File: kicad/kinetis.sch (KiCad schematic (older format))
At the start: 25 parts, among them J1 USB_Micro_B, J2 FTDI_Connector, U1 MKL16Z64VLH4, U2 LM1117-ADJ

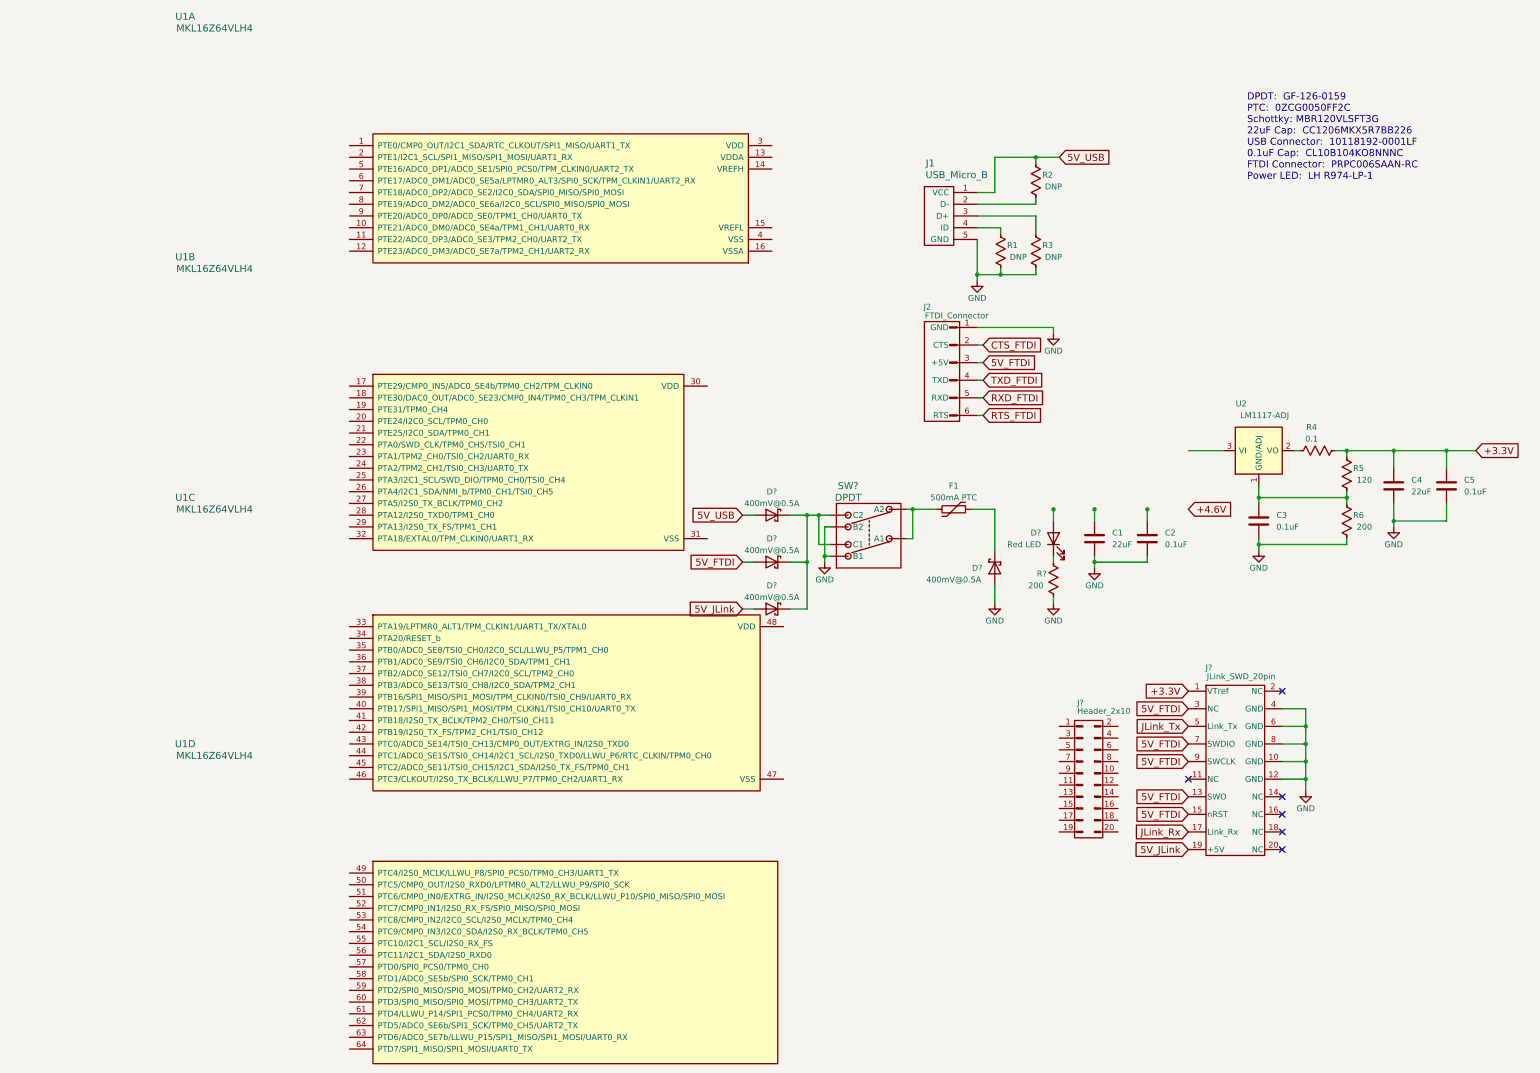
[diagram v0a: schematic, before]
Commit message: Updated schematic. Reworked Kinetis symbol. Connected LEDs.
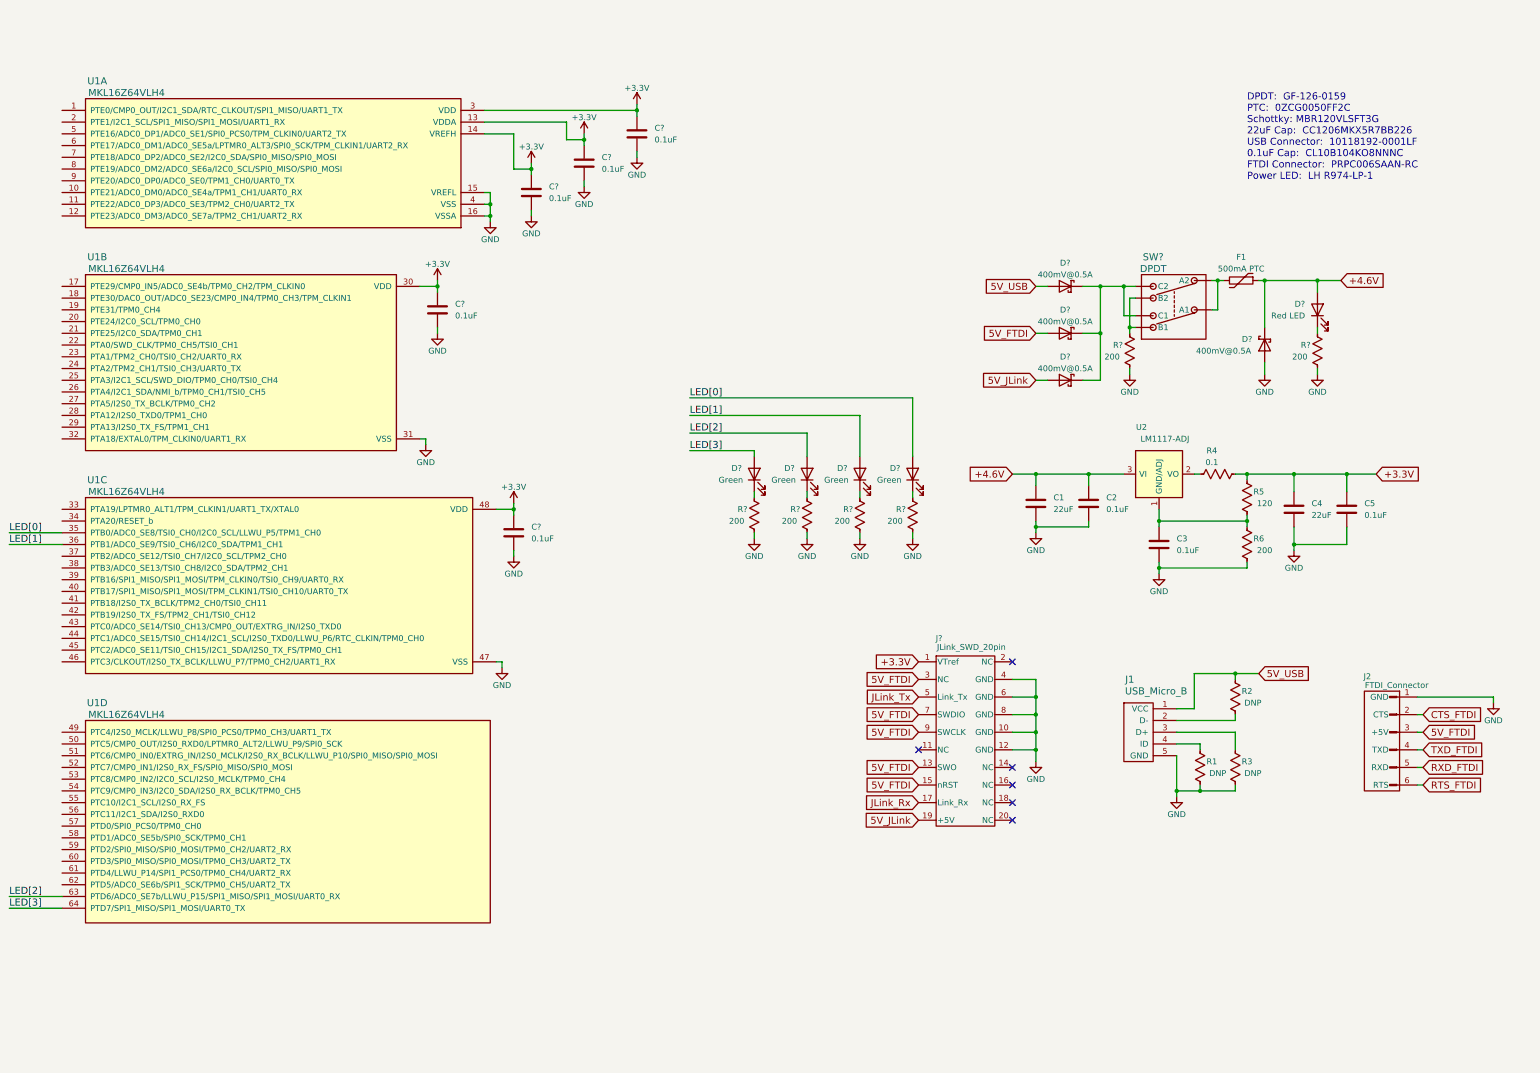
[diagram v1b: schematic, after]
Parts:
- removed J?: Header_2x10, symbol Header_2x10
- added C? (x5): 0.1uF, symbol C
- added D? (x4): Green, symbol LED_AK
- added R? (x5): 200, symbol R_US
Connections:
- net +4.6V: now also C1.1, C2.1, D?.A, D?.K, F1.1, U2.3 (VI)
- net GND: now also U1.15 (VREFL), U1.16 (VSSA), U1.31 (VSS), U1.4 (VSS), U1.47 (VSS), C?.2, C?.2, C?.2, C?.2, C?.2, R?.1, R?.1, R?.1, R?.1, R?.1; no longer SW?.~ (C2)
- net +3V3: now reaches U1.13 (VDDA)
- net +3V3: now also U1.14 (VREFH), U1.3 (VDD), U1.30 (VDD), U1.48 (VDD), C?.1, C?.1, C?.1, C?.1, C?.1
- net LED[0]: now reaches U1.35 (PTB0/ADC0_SE8/TSI0_CH0/I2C0_SCL/LLWU_P5/TPM1_CH0)
- net LED[0]: now also D?.A
- net LED[1]: now reaches U1.36 (PTB1/ADC0_SE9/TSI0_CH6/I2C0_SDA/TPM1_CH1)
- net LED[1]: now also D?.A
- net LED[2]: now reaches U1.63 (PTD6/ADC0_SE7b/LLWU_P15/SPI1_MISO/SPI1_MOSI/UART0_RX)
- net LED[2]: now also D?.A
- net LED[3]: now reaches U1.64 (PTD7/SPI1_MISO/SPI1_MOSI/UART0_TX)
- net LED[3]: now also D?.A
- new net: R?.2, SW?.~ (C2)
- new net: D?.K, R?.2 (x4)
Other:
- moved on the sheet: C1, C2, C3, C4, C5, D?, F1, J1, J2, J?, R1, R2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

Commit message: Lots of changes.
Added clock crystal and load capacitors. Added 16-pin headers to
each side of the microcontroller. Added user pushbuttons and also
a reset pushbutton.
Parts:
- added C6, C7: 27pF, symbol C
- added J1, J2, J3, J4: CONN_01X16, symbol CONN_01X16
- added R1, R10, R11, R12, R13, R14, R2, R3, R4, R5, R6, R7, R8, R9: 0.0, symbol R_US
- added R15, R25, R26, R31, R32: 10k, symbol R_US
- added R16: 120, symbol R_US
- added SW1, SW3, SW4, SW5, SW6: SPST, symbol SPST
- added Y1: 12 MHz, symbol Crystal
- gave numbers to parts that had none: 22
- renumbered C3 to C10, C4 to C11, C5 to C12, C1 to C8, C2 to C9, J1 to J6, J2 to J7, R1 to R21, R2 to R23, R3 to R24, R4 to R27, R5 to R28, R6 to R29
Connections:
- net +3.3V: now also J1.13 (P13), J1.14 (P14), J1.3 (P3), J2.14 (P14), J3.16 (P16)
- net +3V3: now also R15.1, SW3.3, SW3.4, SW4.3, SW4.4, SW5.3, SW5.4, SW6.3, SW6.4
- net 5V_FTDI: no longer J5.13 (SWO), J5.15 (nRST), J5.3 (NC), J5.7 (SWDIO), J5.9 (SWCLK)
- net CTS_FTDI: now also R3.2
- net GND: now also C6.2, C7.2, J1.15 (P15), J1.16 (P16), J1.4 (P4), J2.15 (P15), J3.15 (P15), R25.2, R26.2, R31.2, R32.2, SW1.1, SW1.2
- net JLink_Rx: now also R12.2
- net JLink_Tx: now also R11.2
- net LED[0]: now also R5.2; no longer U1.35 (PTB0/ADC0_SE8/TSI0_CH0/I2C0_SCL/LLWU_P5/TPM1_CH0)
- net LED[1]: now also R6.2; no longer U1.36 (PTB1/ADC0_SE9/TSI0_CH6/I2C0_SDA/TPM1_CH1)
- net LED[2]: now also R13.2; no longer U1.63 (PTD6/ADC0_SE7b/LLWU_P15/SPI1_MISO/SPI1_MOSI/UART0_RX)
- net LED[3]: now also R14.2; no longer U1.64 (PTD7/SPI1_MISO/SPI1_MOSI/UART0_TX)
- net RTS_FTDI: now also R4.2
- net RXD_FTDI: now also R1.2
- net TXD_FTDI: now also R2.2
- net HEADER_A[1]: now reaches U1.1 (PTE0/CMP0_OUT/I2C1_SDA/RTC_CLKOUT/SPI1_MISO/UART1_TX)
- net HEADER_A[1]: now also J1.1 (P1)
- net HEADER_A[10]: now reaches U1.10 (PTE21/ADC0_DM0/ADC0_SE4a/TPM1_CH1/UART0_RX)
- net HEADER_A[10]: now also J1.10 (P10), R2.1
- net HEADER_A[11]: now reaches U1.11 (PTE22/ADC0_DP3/ADC0_SE3/TPM2_CH0/UART2_TX)
- net HEADER_A[11]: now also J1.11 (P11)
- net HEADER_A[12]: now reaches U1.12 (PTE23/ADC0_DM3/ADC0_SE7a/TPM2_CH1/UART2_RX)
- net HEADER_A[12]: now also J1.12 (P12)
- net HEADER_A[2]: now reaches U1.2 (PTE1/I2C1_SCL/SPI1_MISO/SPI1_MOSI/UART1_RX)
- net HEADER_A[2]: now also J1.2 (P2)
- net HEADER_A[5]: now reaches U1.5 (PTE16/ADC0_DP1/ADC0_SE1/SPI0_PCS0/TPM_CLKIN0/UART2_TX)
- net HEADER_A[5]: now also J1.5 (P5)
- net HEADER_A[6]: now reaches U1.6 (PTE17/ADC0_DM1/ADC0_SE5a/LPTMR0_ALT3/SPI0_SCK/TPM_CLKIN1/UART2_RX)
- net HEADER_A[6]: now also J1.6 (P6)
- net HEADER_A[7]: now reaches U1.7 (PTE18/ADC0_DP2/ADC0_SE2/I2C0_SDA/SPI0_MISO/SPI0_MOSI)
- net HEADER_A[7]: now also J1.7 (P7)
- net HEADER_A[8]: now reaches U1.8 (PTE19/ADC0_DM2/ADC0_SE6a/I2C0_SCL/SPI0_MISO/SPI0_MOSI)
- net HEADER_A[8]: now also J1.8 (P8)
- net HEADER_A[9]: now reaches U1.9 (PTE20/ADC0_DP0/ADC0_SE0/TPM1_CH0/UART0_TX)
- net HEADER_A[9]: now also J1.9 (P9), R1.1
- net HEADER_B[1]: now reaches U1.17 (PTE29/CMP0_IN5/ADC0_SE4b/TPM0_CH2/TPM_CLKIN0)
- net HEADER_B[1]: now also J2.1 (P1)
- net HEADER_B[2]: now reaches U1.18 (PTE30/DAC0_OUT/ADC0_SE23/CMP0_IN4/TPM0_CH3/TPM_CLKIN1)
- net HEADER_B[2]: now also J2.2 (P2)
- net HEADER_B[3]: now reaches U1.19 (PTE31/TPM0_CH4)
- net HEADER_B[3]: now also J2.3 (P3)
- net HEADER_B[4]: now reaches U1.20 (PTE24/I2C0_SCL/TPM0_CH0)
- net HEADER_B[4]: now also J2.4 (P4)
- net HEADER_B[5]: now reaches U1.21 (PTE25/I2C0_SDA/TPM0_CH1)
- net HEADER_B[5]: now also J2.5 (P5)
- net JLink_SWCLK: now reaches U1.22 (PTA0/SWD_CLK/TPM0_CH5/TSI0_CH1)
- net JLink_SWCLK: now also J5.9 (SWCLK)
- net HEADER_B[7]: now reaches U1.23 (PTA1/TPM2_CH0/TSI0_CH2/UART0_RX)
- net HEADER_B[7]: now also J2.7 (P7)
- net HEADER_B[8]: now reaches U1.24 (PTA2/TPM2_CH1/TSI0_CH3/UART0_TX)
- net HEADER_B[8]: now also J2.8 (P8)
- net JLink_SWDIO: now reaches U1.25 (PTA3/I2C1_SCL/SWD_DIO/TPM0_CH0/TSI0_CH4)
- net JLink_SWDIO: now also J5.7 (SWDIO)
- net HEADER_B[10]: now reaches U1.26 (PTA4/I2C1_SDA/NMI_b/TPM0_CH1/TSI0_CH5)
- net HEADER_B[10]: now also J2.10 (P10)
- net HEADER_B[11]: now reaches U1.27 (PTA5/I2S0_TX_BCLK/TPM0_CH2)
- net HEADER_B[11]: now also J2.11 (P11)
- net HEADER_B[12]: now reaches U1.28 (PTA12/I2S0_TXD0/TPM1_CH0)
- net HEADER_B[12]: now also J2.12 (P12), R3.1
- net HEADER_B[13]: now reaches U1.29 (PTA13/I2S0_TX_FS/TPM1_CH1)
- net HEADER_B[13]: now also J2.13 (P13), R4.1
- net EXTAL0: now reaches U1.32 (PTA18/EXTAL0/TPM_CLKIN0/UART1_RX)
- net EXTAL0: now also C6.1, Y1.1
- net XTAL0: now reaches U1.33 (PTA19/LPTMR0_ALT1/TPM_CLKIN1/UART1_TX/XTAL0)
- net XTAL0: now also C7.1, Y1.2
- net JLink_nRST: now reaches U1.34 (PTA20/RESET_b)
- net JLink_nRST: now also J5.15 (nRST), R15.2, R16.1
- net HEADER_C[5]: now reaches U1.37 (PTB2/ADC0_SE12/TSI0_CH7/I2C0_SCL/TPM2_CH0)
- net HEADER_C[5]: now also J3.5 (P5), R7.1
- net HEADER_C[6]: now reaches U1.38 (PTB3/ADC0_SE13/TSI0_CH8/I2C0_SDA/TPM2_CH1)
- net HEADER_C[6]: now also J3.6 (P6), R8.1
- net HEADER_C[7]: now reaches U1.39 (PTB16/SPI1_MISO/SPI1_MOSI/TPM_CLKIN0/TSI0_CH9/UART0_RX)
- net HEADER_C[7]: now also J3.7 (P7), R9.1
- net HEADER_C[8]: now reaches U1.40 (PTB17/SPI1_MISO/SPI1_MOSI/TPM_CLKIN1/TSI0_CH10/UART0_TX)
- net HEADER_C[8]: now also J3.8 (P8), R10.1
- net HEADER_C[9]: now reaches U1.41 (PTB18/I2S0_TX_BCLK/TPM2_CH0/TSI0_CH11)
- net HEADER_C[9]: now also J3.9 (P9)
- net HEADER_C[10]: now reaches U1.42 (PTB19/I2S0_TX_FS/TPM2_CH1/TSI0_CH12)
- net HEADER_C[10]: now also J3.10 (P10)
- net HEADER_C[11]: now reaches U1.43 (PTC0/ADC0_SE14/TSI0_CH13/CMP0_OUT/EXTRG_IN/I2S0_TXD0)
- net HEADER_C[11]: now also J3.11 (P11)
- net HEADER_C[12]: now reaches U1.44 (PTC1/ADC0_SE15/TSI0_CH14/I2C1_SCL/I2S0_TXD0/LLWU_P6/RTC_CLKIN/TPM0_CH0)
- net HEADER_C[12]: now also J3.12 (P12)
- net HEADER_C[13]: now reaches U1.45 (PTC2/ADC0_SE11/TSI0_CH15/I2C1_SDA/I2S0_TX_FS/TPM0_CH1)
- net HEADER_C[13]: now also J3.13 (P13)
- net HEADER_C[14]: now reaches U1.46 (PTC3/CLKOUT/I2S0_TX_BCLK/LLWU_P7/TPM0_CH2/UART1_RX)
- net HEADER_C[14]: now also J3.14 (P14)
- net HEADER_D[1]: now reaches U1.49 (PTC4/I2S0_MCLK/LLWU_P8/SPI0_PCS0/TPM0_CH3/UART1_TX)
- net HEADER_D[1]: now also J4.1 (P1)
- net HEADER_D[2]: now reaches U1.50 (PTC5/CMP0_OUT/I2S0_RXD0/LPTMR0_ALT2/LLWU_P9/SPI0_SCK)
- net HEADER_D[2]: now also J4.2 (P2)
- net HEADER_D[3]: now reaches U1.51 (PTC6/CMP0_IN0/EXTRG_IN/I2S0_MCLK/I2S0_RX_BCLK/LLWU_P10/SPI0_MISO/SPI0_MOSI)
- net HEADER_D[3]: now also J4.3 (P3)
- net HEADER_D[4]: now reaches U1.52 (PTC7/CMP0_IN1/I2S0_RX_FS/SPI0_MISO/SPI0_MOSI)
- net HEADER_D[4]: now also J4.4 (P4)
- net HEADER_D[5]: now reaches U1.53 (PTC8/CMP0_IN2/I2C0_SCL/I2S0_MCLK/TPM0_CH4)
- net HEADER_D[5]: now also J4.5 (P5)
- net HEADER_D[6]: now reaches U1.54 (PTC9/CMP0_IN3/I2C0_SDA/I2S0_RX_BCLK/TPM0_CH5)
- net HEADER_D[6]: now also J4.6 (P6)
- net HEADER_D[7]: now reaches U1.55 (PTC10/I2C1_SCL/I2S0_RX_FS)
- net HEADER_D[7]: now also J4.7 (P7)
- net HEADER_D[8]: now reaches U1.56 (PTC11/I2C1_SDA/I2S0_RXD0)
- net HEADER_D[8]: now also J4.8 (P8)
- net HEADER_D[9]: now reaches U1.57 (PTD0/SPI0_PCS0/TPM0_CH0)
- net HEADER_D[9]: now also J4.9 (P9)
- net HEADER_D[10]: now reaches U1.58 (PTD1/ADC0_SE5b/SPI0_SCK/TPM0_CH1)
- net HEADER_D[10]: now also J4.10 (P10)
- net HEADER_D[11]: now reaches U1.59 (PTD2/SPI0_MISO/SPI0_MOSI/TPM0_CH2/UART2_RX)
- net HEADER_D[11]: now also J4.11 (P11)
- net HEADER_D[12]: now reaches U1.60 (PTD3/SPI0_MISO/SPI0_MOSI/TPM0_CH3/UART2_TX)
- net HEADER_D[12]: now also J4.12 (P12)
- net HEADER_D[13]: now reaches U1.61 (PTD4/LLWU_P14/SPI1_PCS0/TPM0_CH4/UART2_RX)
- net HEADER_D[13]: now also J4.13 (P13), R11.1
- net HEADER_D[14]: now reaches U1.62 (PTD5/ADC0_SE6b/SPI1_SCK/TPM0_CH5/UART2_TX)
- net HEADER_D[14]: now also J4.14 (P14), R12.1
- new net: R16.2, SW1.3, SW1.4
- new net HEADER_C[3]: J3.3 (P3), R5.1, U1.35 (PTB0/ADC0_SE8/TSI0_CH0/I2C0_SCL/LLWU_P5/TPM1_CH0)
- new net HEADER_C[4]: J3.4 (P4), R6.1, U1.36 (PTB1/ADC0_SE9/TSI0_CH6/I2C0_SDA/TPM1_CH1)
- new net HEADER_D[15]: J4.15 (P15), R13.1, U1.63 (PTD6/ADC0_SE7b/LLWU_P15/SPI1_MISO/SPI1_MOSI/UART0_RX)
- new net HEADER_D[16]: J4.16 (P16), R14.1, U1.64 (PTD7/SPI1_MISO/SPI1_MOSI/UART0_TX)
- new net SW[E]: R31.1, R9.2, SW5.1, SW5.2
- new net SW[N]: R25.1, R7.2, SW3.1, SW3.2
- new net SW[S]: R32.1, R8.2, SW6.1, SW6.2
- new net SW[W]: R10.2, R26.1, SW4.1, SW4.2
- no-connect marks 6 -> 13
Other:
- note added: "DPDT: GF-126-0159\nPTC: 0ZCG0050FF2C\nSchottky: MBR120VLSFT3G\n22uF Cap: CC1206MKX5R7BB226\nUSB Connector: 10118192-0001LF\n0.1uF Cap: CL10B104KO8NNNC\nFTDI Connector: PRPC006SAAN-RC\nPower LED: LH R974-LP-1\nCrystal: ABLS2-12.000MHZ-D4Y-T\nCrystal Caps: CL10C270JB8NNNC\n"
- note removed: "DPDT: GF-126-0159\nPTC: 0ZCG0050FF2C\nSchottky: MBR120VLSFT3G\n22uF Cap: CC1206MKX5R7BB226\nUSB Connector: 10118192-0001LF\n0.1uF Cap: CL10B104KO8NNNC\nFTDI Connector: PRPC006SAAN-RC\nPower LED: LH R974-LP-1"
- moved on the sheet: C1, C10, C11, C12, C2, C3, C4, C5, C8, C9, D1, D2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

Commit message: Schematic cleanups and part number annotations.
This commit cleans up a lot of drafting nits, and also adds custom
'Manufacturer' and 'Manufacturer PN' fields.
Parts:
- removed J5: JLink_SWD_20pin, symbol JLink_SWD_20pin
- removed J6: USB_Micro_B, symbol USB_Micro_B
- removed J7: FTDI_Connector, symbol FTDI_Connector
- removed R1, R10, R11, R12, R13, R14, R2, R3, R4, R5, R6, R7, R8, R9: 0.0, symbol R_US
- removed R15, R25, R26, R31, R32: 10k, symbol R_US
- removed R16, R28: 120, symbol R_US
- removed R17, R18, R19, R20, R22, R29, R30: 200, symbol R_US
- removed R21, R23, R24: DNP, symbol R_US
- removed R27: 0.1, symbol R_US
- removed SW6: SPST, symbol SPST
- removed U2: LM1117-ADJ, symbol LM1117-ADJ
- added J5: USB_Micro_B, symbol USB_Micro_B
- added J6: FTDI_Connector, symbol FTDI_Connector
- added J7: JLink_SWD_20pin, symbol JLink_SWD_20pin
- added R1, R10, R11, R12, R13, R14, R2, R29, R3, R4, R5, R6, R7, R8, R9: 0.1, SM_0805, symbol R
- added R15, R18, R19, R20, R23, R31, R32: 200, SM_0805, symbol R
- added R16, R17, R21, R22, R25: 10k, SM_0805, symbol R
- added R24, R26, R27: DNP, SM_0805, symbol R
- added R28, R30: 120, SM_0805, symbol R
- added SW2: SPST, symbol SPST
- added U2: LM1117-ADJ, SOT-223, symbol LM1117-ADJ-RESCUE-kinetis
- C1, C10, C12, C2, C3, C4, C9: footprint (none) -> SM_0603; Manufacturer (none) -> Samsung; Manufacturer PN (none) -> CL10B104KO8NNNC
- C11, C8: footprint (none) -> SM_1206; Manufacturer (none) -> Yageo; Manufacturer PN (none) -> CC1206MKX5R7BB226
- C5: value 0.1uF -> 27pF; footprint (none) -> SM_0603; Manufacturer (none) -> Samsung; Manufacturer PN (none) -> CL10C270JB8NNNC
- C6: value 27pF -> 0.1uF; footprint (none) -> SM_0603; Manufacturer (none) -> Samsung; Manufacturer PN (none) -> CL10B104KO8NNNC
- C7: footprint (none) -> SM_0603; Manufacturer (none) -> Samsung; Manufacturer PN (none) -> CL10C270JB8NNNC
- D1, D2, D3, D4: footprint (none) -> D_0805; Manufacturer (none) -> OSRAM; Manufacturer PN (none) -> LG R971-KN-1
- D5, D6, D7, D8: footprint (none) -> SOD-123F; Manufacturer (none) -> ON Semi; Manufacturer PN (none) -> MBR120VLSFT3G
- D9: value Red LED -> Red; footprint (none) -> D_0805; Manufacturer (none) -> OSRAM; Manufacturer PN (none) -> LH R974-LP-1
- F1: footprint (none) -> SM_1812; Manufacturer (none) -> Bel Fuse; Manufacturer PN (none) -> 0ZCG0050FF2C
- J1, J2, J3, J4: Manufacturer (none) -> Sullins; Manufacturer PN (none) -> PRPC016SAAN-RC
- SW1, SW3, SW4, SW5: Manufacturer (none) -> C&K; Manufacturer PN (none) -> PTS645SM43SMTR92 LFS
- U1: footprint (none) -> LFQP-64; Manufacturer (none) -> NXP; Manufacturer PN (none) -> MKL16Z64VLH4
- Y1: value 12 MHz -> 12.000 MHz; footprint (none) -> HC49/US; Manufacturer (none) -> Abracon; Manufacturer PN (none) -> ABLS2-12.000MHZ-D4Y-T
- renumbered SW2 to SW6
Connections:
- net +3.3V: now also J7.1 (VTref); no longer C11.1, C12.1
- net +3V3: now also C11.1, C12.1, C6.1, SW1.1, SW1.2, SW3.1, SW3.2, SW4.1, SW4.2, R25.1, R29.2, R30.1, SW2.1, SW2.2; no longer C5.1, SW3.3, SW3.4, SW4.3, SW4.4, SW5.3, SW5.4
- net +4.6V: now also U2.3 (VI)
- net 5V_FTDI: now also J6.3 (+5V)
- net 5V_JLink: now also J7.19 (+5V)
- net 5V_USB: now also J5.1 (VCC), R26.1
- net CTS_FTDI: now also J6.2 (CTS), R3.1
- net EXTAL0: now also C5.1; no longer C6.1
- net GND: now also SW5.1, SW5.2, J5.5 (GND), J6.1 (GND), J7.10 (GND), J7.12 (GND), J7.4 (GND), J7.6 (GND), J7.8 (GND), R15.2, R16.2, R17.2, R18.2, R19.2, R20.2, R21.2, R22.2, R23.2, R24.2, R27.2, R31.2, R32.2; no longer SW1.1, SW1.2
- net HEADER_A[10]: now also R2.2
- net HEADER_A[9]: now also R1.2
- net HEADER_B[12]: now also R3.2
- net HEADER_B[13]: now also R4.2
- net HEADER_C[3]: now also R5.2
- net HEADER_C[4]: now also R6.2
- net HEADER_C[5]: now also R7.2
- net HEADER_C[6]: now also R8.2
- net HEADER_C[7]: now also R9.2
- net HEADER_C[8]: now also R10.2
- net HEADER_D[13]: now also R11.2
- net HEADER_D[14]: now also R12.2
- net HEADER_D[15]: now also R13.2
- net HEADER_D[16]: now also R14.2
- net JLink_Rx: now also J7.17 (Link_Rx), R12.1
- net JLink_SWCLK: now also J7.9 (SWCLK)
- net JLink_SWDIO: now also J7.7 (SWDIO)
- net JLink_Tx: now also J7.5 (Link_Tx), R11.1
- net JLink_nRST: now also J7.15 (nRST), R25.2, R28.1
- net LED[0]: now also R5.1
- net LED[1]: now also R6.1
- net LED[2]: now also R13.1
- net LED[3]: now also R14.1
- net RTS_FTDI: now also J6.6 (RTS), R4.1
- net RXD_FTDI: now also J6.5 (RXD), R1.1
- net SW[E]: now also SW3.3, SW3.4, R21.1, R9.1; no longer SW5.1, SW5.2
- net SW[N]: now also SW1.3, SW1.4, R16.1, R7.1; no longer SW3.1, SW3.2
- net SW[S]: now also SW4.3, SW4.4, R22.1, R8.1
- net SW[W]: now also R10.1, R17.1, SW2.3, SW2.4; no longer SW4.1, SW4.2
- net TXD_FTDI: now also J6.4 (TXD), R2.1
- net at C10.1: now also R30.2, R31.1, U2.1 (GND/ADJ)
- net at SW6.~ (C2): now also R23.1
- net at D9.K: now also R32.1
- net at D1.K: now also R15.1
- net at D2.K: now also R18.1
- net at D3.K: now also R19.1
- net at D4.K: now also R20.1
- new net: R29.1, U2.2 (VO), U2.4 (VO)
- new net: J5.2 (D-), R26.2
- new net: J5.3 (D+), R27.1
- new net: J5.4 (ID), R24.1
- new net: R28.2, SW5.3, SW5.4
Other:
- note added: "Header for 6-pin Sparkfun\nor Adafruit USB-UART cable."
- note added: "Header for Segger\nJ-Link Debugger"
- note added: "USB Micro-B connector.\nUsed for power only."
- moved on the sheet: SW6

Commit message: Cosmetic cleanups and library tweaks.
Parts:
- removed D2, D3, D4: Green, D_0805, symbol LED_AK
- added D2, D3, D4: Green, D_0805, symbol LED
- D1, D9: symbol LED_AK -> LED
- U2: symbol LM1117-ADJ-RESCUE-kinetis -> LM1117-ADJ
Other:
- note removed: "DPDT: GF-126-0159\nPTC: 0ZCG0050FF2C\nSchottky: MBR120VLSFT3G\n22uF Cap: CC1206MKX5R7BB226\nUSB Connector: 10118192-0001LF\n0.1uF Cap: CL10B104KO8NNNC\nFTDI Connector: PRPC006SAAN-RC\nPower LED: LH R974-LP-1\nCrystal: ABLS2-12.000MHZ-D4Y-T\nCrystal Caps: CL10C270JB8NNNC\n"

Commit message: Added some footprints and changed crystal footprint name.
This commit adds a little over half of the design's required footprints,
and also changes the name of the crystal footprint to avoid ambiguity
with the through-hole flavors of HC49/US.
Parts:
- Y1: footprint HC49/US -> SM_HC49US
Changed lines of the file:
@@
 F 0 "Y1" H 9700 3050 50  0000 L CNN
 F 1 "12.000 MHz" H 9550 2950 50  0000 L CNN
-F 2 "HC49/US" H 9750 2800 50  0001 C CNN
+F 2 "SM_HC49US" H 9750 2800 50  0001 C CNN
 F 3 "" H 9750 2950 50  0001 C CNN
 F 4 "Abracon" H 9850 3150 60  0001 C CNN "Manufacturer"
